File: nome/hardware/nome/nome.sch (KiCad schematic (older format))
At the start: 50 parts, among them J1 Audio-Jack-3_2Switches, J2 Conn_02x05_Odd_Even, J3 Barrel_Jack, SW1 SW_SPST, SW2 Rotary_Encoder_Switch, U1 LM1117-1.8, U2 LM1117-3.3, U3 AS1115, U4 STMF411CEU6, U5 LTC-4727JS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

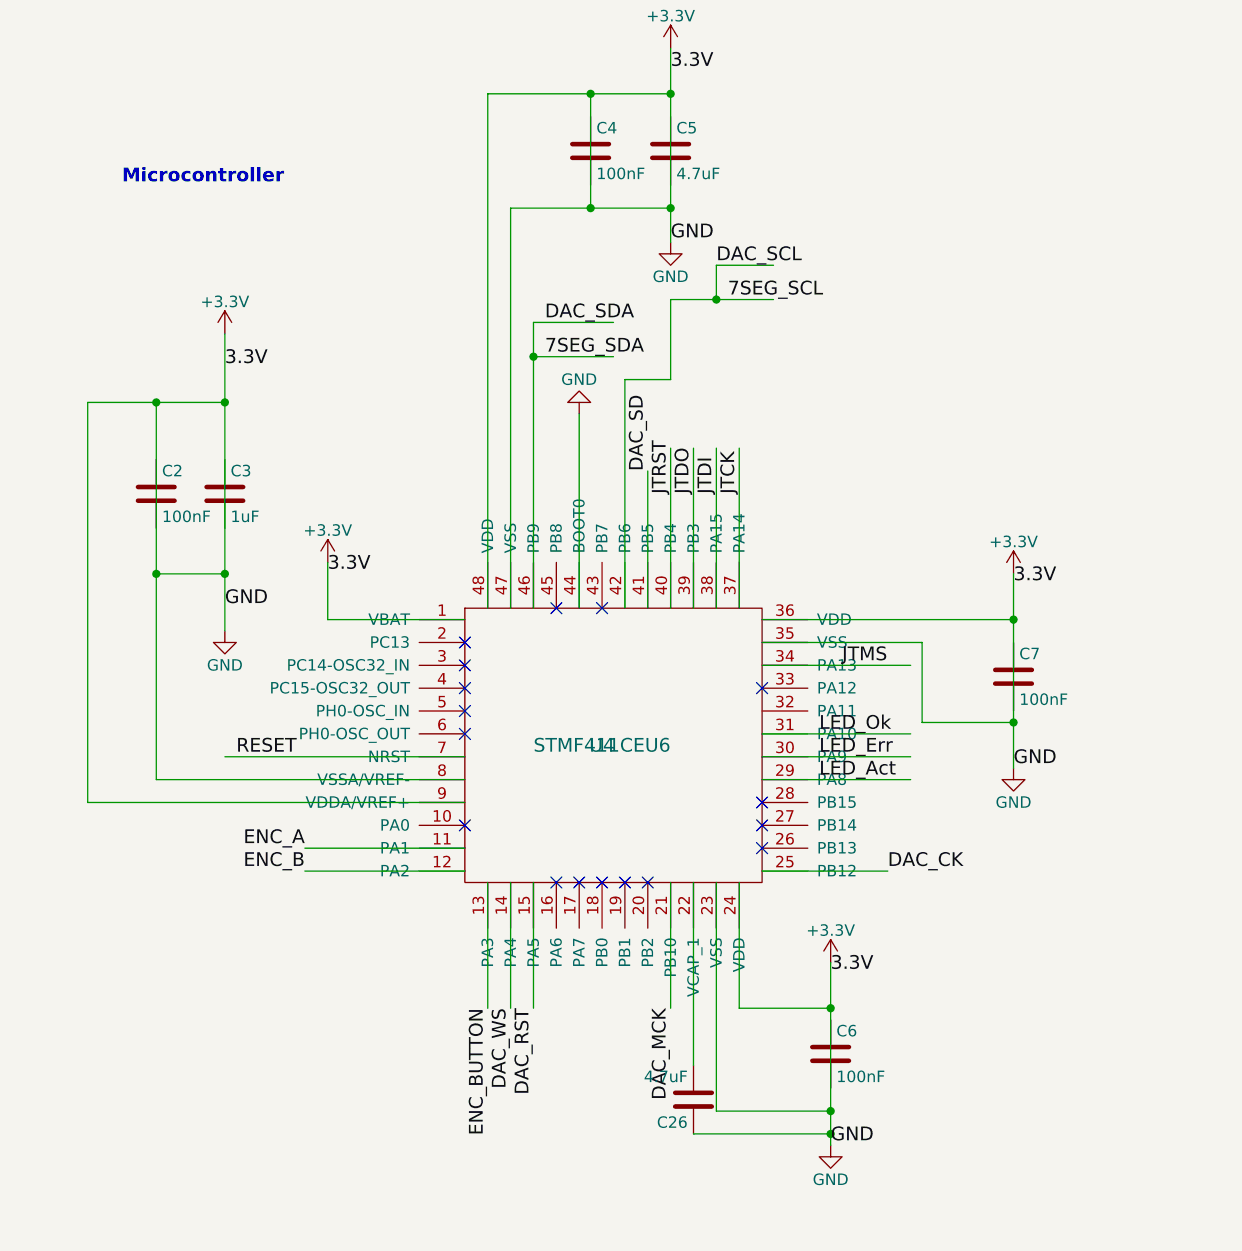
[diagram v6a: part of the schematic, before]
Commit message: Add in capacitor footprints
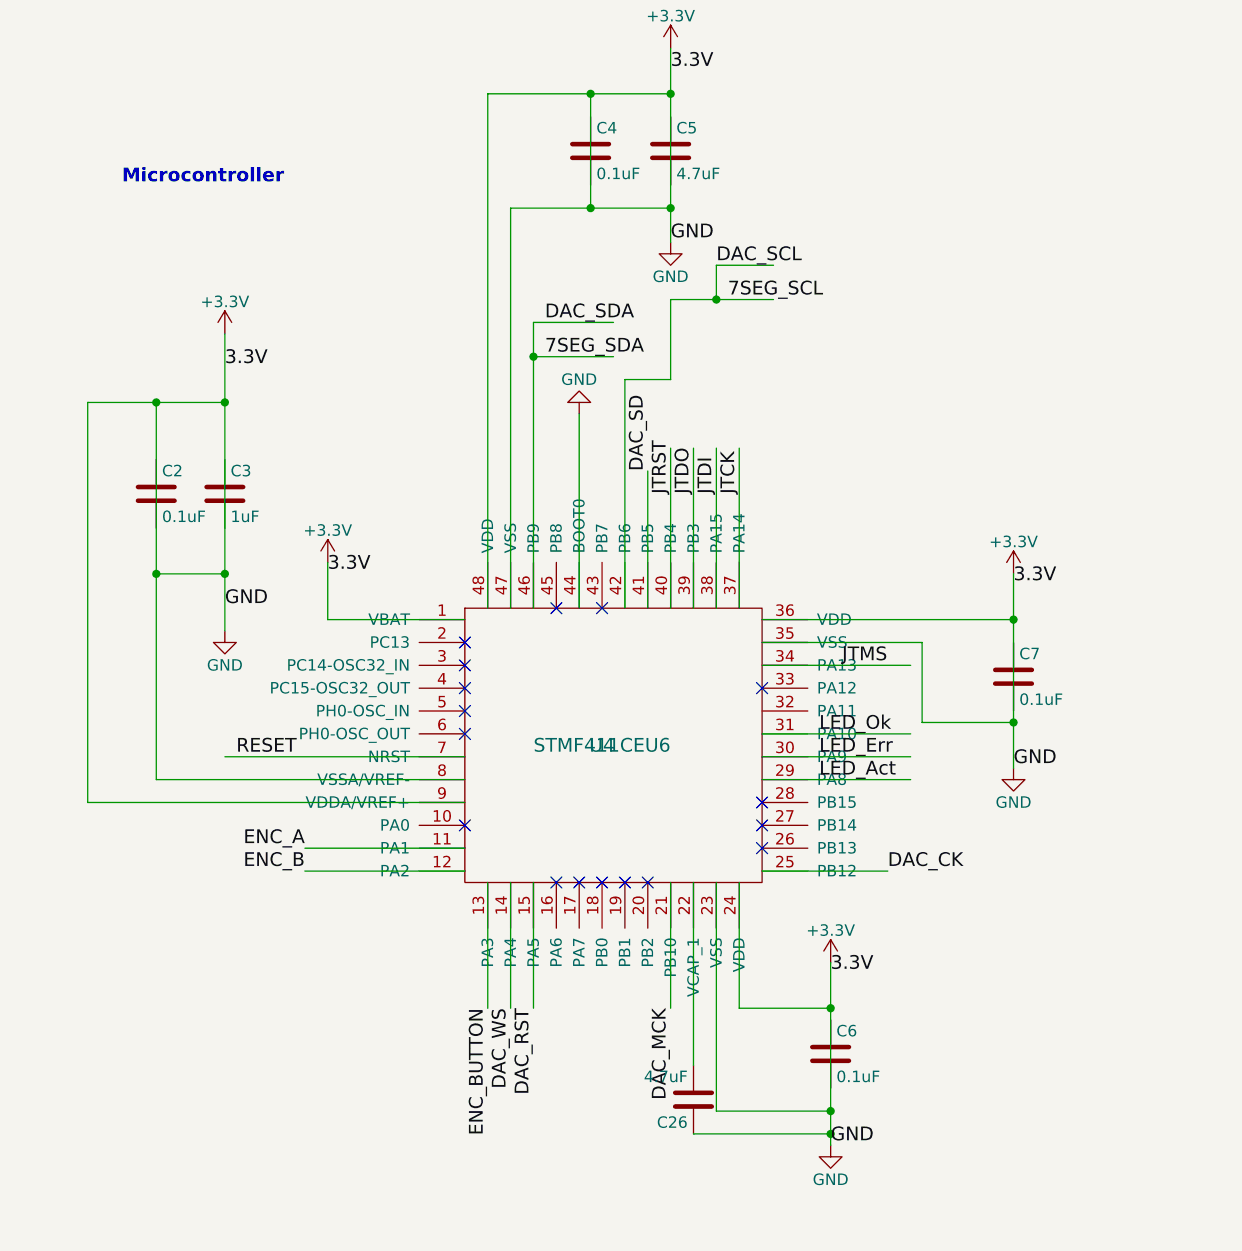
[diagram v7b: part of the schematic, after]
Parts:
- C1, C10, C11, C12, C13, C14, C15, C16, C17, C18, C19, C20, C21, C22, C23, C24, C25, C26, C3, C5, C8, C9: footprint (none) -> Capacitors_SMD:C_0805_HandSoldering
- C2, C4, C6, C7: value 100nF -> 0.1uF; footprint (none) -> Capacitors_SMD:C_0805_HandSoldering
- R1, R2, R3, R4, R5, R6, R7: footprint (none) -> Resistors_SMD:R_0805_HandSoldering
- U1, U2: footprint (none) -> TO_SOT_Packages_SMD:SOT-223
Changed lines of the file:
@@
 P 4700 5500
 F 0 "C6" H 4725 5600 50  0000 L CNN
-F 1 "100nF" H 4725 5400 50  0000 L CNN
-F 2 "" H 4738 5350 50  0001 C CNN
+F 1 "0.1uF" H 4725 5400 50  0000 L CNN
+F 2 "Capacitors_SMD:C_0805_HandSoldering" H 4738 5350 50  0001 C CNN
 F 3 "" H 4700 5500 50  0001 C CNN
 	1    4700 5500
@@
 P 5500 3850
 F 0 "C7" H 5525 3950 50  0000 L CNN
-F 1 "100nF" H 5525 3750 50  0000 L CNN
-F 2 "" H 5538 3700 50  0001 C CNN
+F 1 "0.1uF" H 5525 3750 50  0000 L CNN
+F 2 "Capacitors_SMD:C_0805_HandSoldering" H 5538 3700 50  0001 C CNN
 F 3 "" H 5500 3850 50  0001 C CNN
 	1    5500 3850
@@
 F 0 "C5" H 4025 1650 50  0000 L CNN
 F 1 "4.7uF" H 4025 1450 50  0000 L CNN
-F 2 "" H 4038 1400 50  0001 C CNN
+F 2 "Capacitors_SMD:C_0805_HandSoldering" H 4038 1400 50  0001 C CNN
 F 3 "" H 4000 1550 50  0001 C CNN
 	1    4000 1550
@@
 P 3650 1550
 F 0 "C4" H 3675 1650 50  0000 L CNN
-F 1 "100nF" H 3675 1450 50  0000 L CNN
-F 2 "" H 3688 1400 50  0001 C CNN
+F 1 "0.1uF" H 3675 1450 50  0000 L CNN
+F 2 "Capacitors_SMD:C_0805_HandSoldering" H 3688 1400 50  0001 C CNN
 F 3 "" H 3650 1550 50  0001 C CNN
 	1    3650 1550
@@
 F 0 "C3" H 2075 3150 50  0000 L CNN
 F 1 "1uF" H 2075 2950 50  0000 L CNN
-F 2 "" H 2088 2900 50  0001 C CNN
+F 2 "Capacitors_SMD:C_0805_HandSoldering" H 2088 2900 50  0001 C CNN
 F 3 "" H 2050 3050 50  0001 C CNN
 	1    2050 3050
@@
 P 1750 3050
 F 0 "C2" H 1775 3150 50  0000 L CNN
-F 1 "100nF" H 1775 2950 50  0000 L CNN
-F 2 "" H 1788 2900 50  0001 C CNN
+F 1 "0.1uF" H 1775 2950 50  0000 L CNN
+F 2 "Capacitors_SMD:C_0805_HandSoldering" H 1788 2900 50  0001 C CNN
 F 3 "" H 1750 3050 50  0001 C CNN
 	1    1750 3050
@@
 F 0 "C15" H 9075 5050 50  0000 L CNN
 F 1 "1uF" H 9075 4850 50  0000 L CNN
-F 2 "" H 9088 4800 50  0001 C CNN
+F 2 "Capacitors_SMD:C_0805_HandSoldering" H 9088 4800 50  0001 C CNN
 F 3 "" H 9050 4950 50  0001 C CNN
 	1    9050 4950
@@
 F 0 "C13" H 8175 4600 50  0000 L CNN
 F 1 "1uF" H 8175 4400 50  0000 L CNN
-F 2 "" H 8188 4350 50  0001 C CNN
+F 2 "Capacitors_SMD:C_0805_HandSoldering" H 8188 4350 50  0001 C CNN
 F 3 "" H 8150 4500 50  0001 C CNN
 	1    8150 4500
@@
 F 0 "C19" H 10275 2100 50  0000 L CNN
 F 1 "0.1uF" H 10275 1900 50  0000 L CNN
-F 2 "" H 10288 1850 50  0001 C CNN
+F 2 "Capacitors_SMD:C_0805_HandSoldering" H 10288 1850 50  0001 C CNN
 F 3 "" H 10250 2000 50  0001 C CNN
 	1    10250 2000
@@
 F 0 "C23" H 11175 2800 50  0000 L CNN
 F 1 "1uF" H 11175 2600 50  0000 L CNN
-F 2 "" H 11188 2550 50  0001 C CNN
+F 2 "Capacitors_SMD:C_0805_HandSoldering" H 11188 2550 50  0001 C CNN
 F 3 "" H 11150 2700 50  0001 C CNN
 	1    11150 2700
@@
 F 0 "C21" H 10725 2800 50  0000 L CNN
 F 1 "0.1uF" H 10725 2600 50  0000 L CNN
-F 2 "" H 10738 2550 50  0001 C CNN
+F 2 "Capacitors_SMD:C_0805_HandSoldering" H 10738 2550 50  0001 C CNN
 F 3 "" H 10700 2700 50  0001 C CNN
 	1    10700 2700
@@
 F 0 "C8" H 7525 4000 50  0000 L CNN
 F 1 "10uF" H 7525 3800 50  0000 L CNN
-F 2 "" H 7538 3750 50  0001 C CNN
+F 2 "Capacitors_SMD:C_0805_HandSoldering" H 7538 3750 50  0001 C CNN
 F 3 "" H 7500 3900 50  0001 C CNN
 	1    7500 3900
@@
 F 0 "C11" H 7925 3150 50  0000 L CNN
 F 1 "0.1uF" H 7925 2950 50  0000 L CNN
-F 2 "" H 7938 2900 50  0001 C CNN
+F 2 "Capacitors_SMD:C_0805_HandSoldering" H 7938 2900 50  0001 C CNN
 F 3 "" H 7900 3050 50  0001 C CNN
 	1    7900 3050
@@
 F 0 "C12" H 7925 4050 50  0000 L CNN
 F 1 "0.1uF" H 7925 3850 50  0000 L CNN
-F 2 "" H 7938 3800 50  0001 C CNN
+F 2 "Capacitors_SMD:C_0805_HandSoldering" H 7938 3800 50  0001 C CNN
 F 3 "" H 7900 3950 50  0001 C CNN
 	1    7900 3950
@@
 F 0 "C24" H 11425 5150 50  0000 L CNN
 F 1 "10uF" H 11425 4950 50  0000 L CNN
-F 2 "" H 11438 4900 50  0001 C CNN
+F 2 "Capacitors_SMD:C_0805_HandSoldering" H 11438 4900 50  0001 C CNN
 F 3 "" H 11400 5050 50  0001 C CNN
 	1    11400 5050
@@
 F 0 "C22" H 10825 5200 50  0000 L CNN
 F 1 "1uF" H 10825 5000 50  0000 L CNN
-F 2 "" H 10838 4950 50  0001 C CNN
+F 2 "Capacitors_SMD:C_0805_HandSoldering" H 10838 4950 50  0001 C CNN
 F 3 "" H 10800 5100 50  0001 C CNN
 	1    10800 5100
@@
 F 0 "C18" H 10225 5750 50  0000 L CNN
 F 1 "150pF" H 10225 5550 50  0000 L CNN
-F 2 "" H 10238 5500 50  0001 C CNN
+F 2 "Capacitors_SMD:C_0805_HandSoldering" H 10238 5500 50  0001 C CNN
 F 3 "" H 10200 5650 50  0001 C CNN
 	1    10200 5650
@@
 F 0 "C20" H 10575 5750 50  0000 L CNN
 F 1 "150pF" H 10575 5550 50  0000 L CNN
-F 2 "" H 10588 5500 50  0001 C CNN
+F 2 "Capacitors_SMD:C_0805_HandSoldering" H 10588 5500 50  0001 C CNN
 F 3 "" H 10550 5650 50  0001 C CNN
 	1    10550 5650
@@
 F 0 "C14" H 8725 6000 50  0000 L CNN
 F 1 "1uF" H 8725 5800 50  0000 L CNN
-F 2 "" H 8738 5750 50  0001 C CNN
+F 2 "Capacitors_SMD:C_0805_HandSoldering" H 8738 5750 50  0001 C CNN
 F 3 "" H 8700 5900 50  0001 C CNN
 	1    8700 5900
@@
 F 0 "C16" H 9125 6000 50  0000 L CNN
 F 1 "0.1uF" H 9125 5800 50  0000 L CNN
-F 2 "" H 9138 5750 50  0001 C CNN
+F 2 "Capacitors_SMD:C_0805_HandSoldering" H 9138 5750 50  0001 C CNN
 F 3 "" H 9100 5900 50  0001 C CNN
 	1    9100 5900
@@
 F 0 "C17" H 9575 5950 50  0000 L CNN
 F 1 "0.1uF" H 9575 5750 50  0000 L CNN
-F 2 "" H 9588 5700 50  0001 C CNN
+F 2 "Capacitors_SMD:C_0805_HandSoldering" H 9588 5700 50  0001 C CNN
 F 3 "" H 9550 5850 50  0001 C CNN
 	1    9550 5850
@@
 F 0 "C9" H 13275 1850 50  0000 L CNN
 F 1 "0.022uF" H 13275 1650 50  0000 L CNN
-F 2 "" H 13288 1600 50  0001 C CNN
+F 2 "Capacitors_SMD:C_0805_HandSoldering" H 13288 1600 50  0001 C CNN
 F 3 "" H 13250 1750 50  0001 C CNN
 	1    13250 1750
@@
 F 0 "R6" V 13730 1750 50  0000 C CNN
 F 1 "51.1" V 13650 1750 50  0000 C CNN
-F 2 "" V 13580 1750 50  0001 C CNN
+F 2 "Resistors_SMD:R_0805_HandSoldering" V 13580 1750 50  0001 C CNN
 F 3 "" H 13650 1750 50  0001 C CNN
 	1    13650 1750
@@
 F 0 "C10" H 13275 2550 50  0000 L CNN
 F 1 "0.022uF" H 13275 2350 50  0000 L CNN
-F 2 "" H 13288 2300 50  0001 C CNN
+F 2 "Capacitors_SMD:C_0805_HandSoldering" H 13288 2300 50  0001 C CNN
 F 3 "" H 13250 2450 50  0001 C CNN
 	1    13250 2450
@@
 F 0 "R7" V 13730 2450 50  0000 C CNN
 F 1 "51.1" V 13650 2450 50  0000 C CNN
-F 2 "" V 13580 2450 50  0001 C CNN
+F 2 "Resistors_SMD:R_0805_HandSoldering" V 13580 2450 50  0001 C CNN
 F 3 "" H 13650 2450 50  0001 C CNN
 	1    13650 2450
@@
 F 0 "U1" H 2350 10875 50  0000 C CNN
 F 1 "LM1117-1.8" H 2500 10875 50  0000 L CNN
-F 2 "" H 2500 10750 50  0001 C CNN
+F 2 "TO_SOT_Packages_SMD:SOT-223" H 2500 10750 50  0001 C CNN
 F 3 "" H 2500 10750 50  0001 C CNN
 	1    2500 10750
@@
 F 0 "U2" H 2350 11725 50  0000 C CNN
 F 1 "LM1117-3.3" H 2500 11725 50  0000 L CNN
-F 2 "" H 2500 11600 50  0001 C CNN
+F 2 "TO_SOT_Packages_SMD:SOT-223" H 2500 11600 50  0001 C CNN
 F 3 "" H 2500 11600 50  0001 C CNN
 	1    2500 11600
@@
 F 0 "R1" V 2680 7100 50  0000 C CNN
 F 1 "10k" V 2600 7100 50  0000 C CNN
-F 2 "" V 2530 7100 50  0001 C CNN
+F 2 "Resistors_SMD:R_0805_HandSoldering" V 2530 7100 50  0001 C CNN
 F 3 "" H 2600 7100 50  0001 C CNN
 	1    2600 7100
@@
 F 0 "C1" H 1475 7900 50  0000 L CNN
 F 1 "0.1uF" H 1475 7700 50  0000 L CNN
-F 2 "" H 1488 7650 50  0001 C CNN
+F 2 "Capacitors_SMD:C_0805_HandSoldering" H 1488 7650 50  0001 C CNN
 F 3 "" H 1450 7800 50  0001 C CNN
 	1    1450 7800
@@
 F 0 "R2" V 10980 8900 50  0000 C CNN
 F 1 "25" V 10900 8900 50  0000 C CNN
-F 2 "" V 10830 8900 50  0001 C CNN
+F 2 "Resistors_SMD:R_0805_HandSoldering" V 10830 8900 50  0001 C CNN
 F 3 "" H 10900 8900 50  0001 C CNN
 	1    10900 8900
@@
 F 0 "R3" V 11280 8900 50  0000 C CNN
 F 1 "40" V 11200 8900 50  0000 C CNN
-F 2 "" V 11130 8900 50  0001 C CNN
+F 2 "Resistors_SMD:R_0805_HandSoldering" V 11130 8900 50  0001 C CNN
 F 3 "" H 11200 8900 50  0001 C CNN
 	1    11200 8900
@@
 F 0 "R4" V 11580 8900 50  0000 C CNN
 F 1 "40" V 11500 8900 50  0000 C CNN
-F 2 "" V 11430 8900 50  0001 C CNN
+F 2 "Resistors_SMD:R_0805_HandSoldering" V 11430 8900 50  0001 C CNN
 F 3 "" H 11500 8900 50  0001 C CNN
 	1    11500 8900
@@
 F 0 "R5" V 11880 8900 50  0000 C CNN
 F 1 "40" V 11800 8900 50  0000 C CNN
-F 2 "" V 11730 8900 50  0001 C CNN
+F 2 "Resistors_SMD:R_0805_HandSoldering" V 11730 8900 50  0001 C CNN
 F 3 "" H 11800 8900 50  0001 C CNN
 	1    11800 8900
@@
 F 0 "C25" H 5975 11800 50  0000 L CNN
 F 1 "0.1uF" H 5975 11600 50  0000 L CNN
-F 2 "" H 5988 11550 50  0001 C CNN
+F 2 "Capacitors_SMD:C_0805_HandSoldering" H 5988 11550 50  0001 C CNN
 F 3 "" H 5950 11700 50  0001 C CNN
 	1    5950 11700
@@
 F 0 "C26" H 4125 5800 50  0000 L CNN
 F 1 "4.7uF" H 4125 5600 50  0000 L CNN
-F 2 "" H 4138 5550 50  0001 C CNN
+F 2 "Capacitors_SMD:C_0805_HandSoldering" H 4138 5550 50  0001 C CNN
 F 3 "" H 4100 5700 50  0001 C CNN
 	1    4100 5700

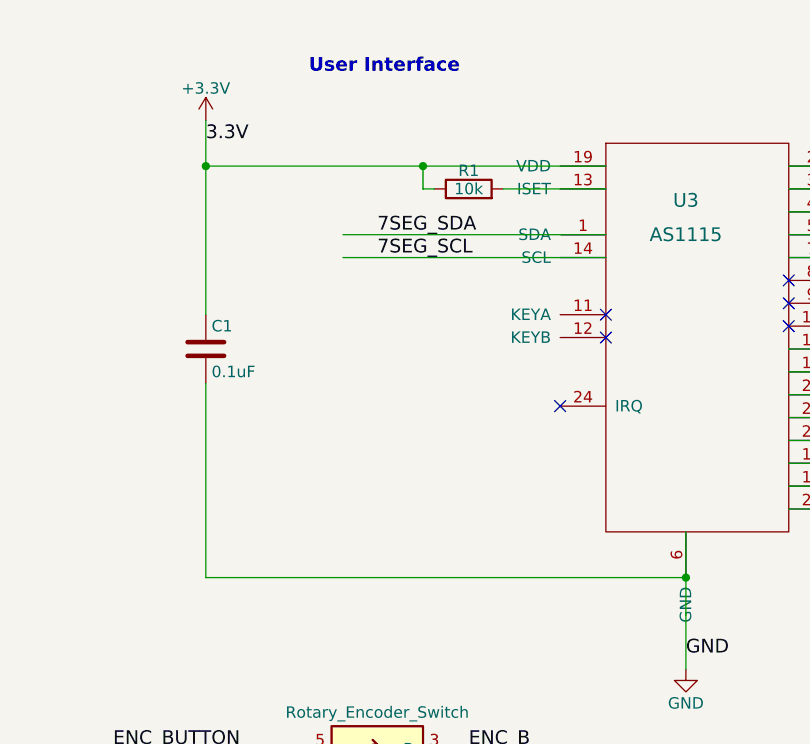
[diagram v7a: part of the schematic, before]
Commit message: Add display I2C pinout
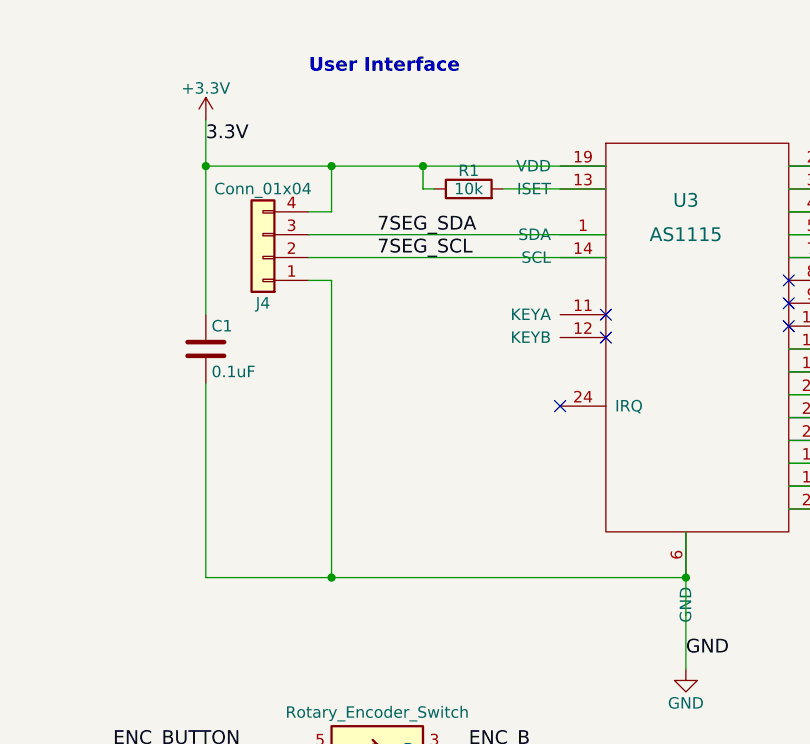
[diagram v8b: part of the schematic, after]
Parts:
- added J4: Conn_01x04, Pin_Headers:Pin_Header_Straight_1x04_Pitch2.54mm, symbol Conn_01x04
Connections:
- wire segments 225 -> 229
